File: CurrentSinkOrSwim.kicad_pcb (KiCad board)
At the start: 2 copper layers, 22 parts, among them P101 CONN_01X03, P102 CONN_01X02, P103 CONN_01X02, Q201 BUK9575, U201 LMV358, U401 LM2931D-R

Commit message: Rough board layout
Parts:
- added P201: CONN_01X01, CSOS Local:FA-220-38E, B.Cu at (116.8, 54.6)
- Q201: moved to B.Cu
- moved R303 69.3 mm to (99.1, 58.4)
- moved R301 65.1 mm to (99.1, 61.0), turned to 180 degrees
- moved R402 61.4 mm to (99.1, 44.5), turned to 270 degrees
- moved P103 57.3 mm to (124.5, 76.2), turned to 180 degrees
- moved R403 53.9 mm to (120.7, 50.8)
- moved P102 53.8 mm to (118.1, 76.2), turned to 180 degrees
- moved U401 53.0 mm to (105.4, 45.7), turned to 90 degrees
- moved R302 52.7 mm to (115.6, 50.8)
- moved P101 51.5 mm to (110.5, 76.2), turned to 180 degrees
- moved D301 45.7 mm to (125.7, 44.5), turned to 180 degrees
- moved R201 43.3 mm to (105.4, 50.8)
- moved R202 43.1 mm to (100.3, 54.6)
- moved R401 42.4 mm to (120.7, 53.3), turned to 180 degrees
- moved C301 42.2 mm to (132.1, 47.0)
- moved C402 39.8 mm to (99.1, 64.8)
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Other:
- board outline added: 43.2 x 41.9 mm

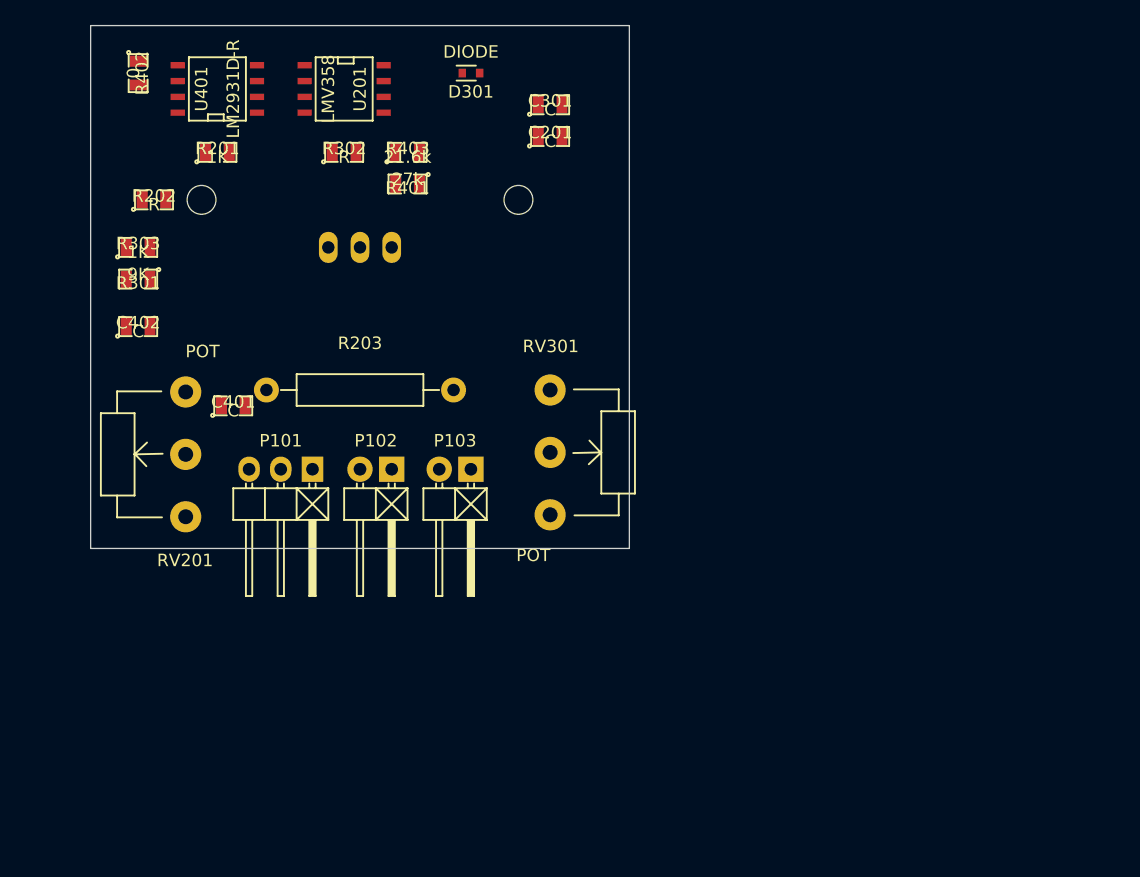
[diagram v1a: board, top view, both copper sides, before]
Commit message: Updated the POT references and schematic
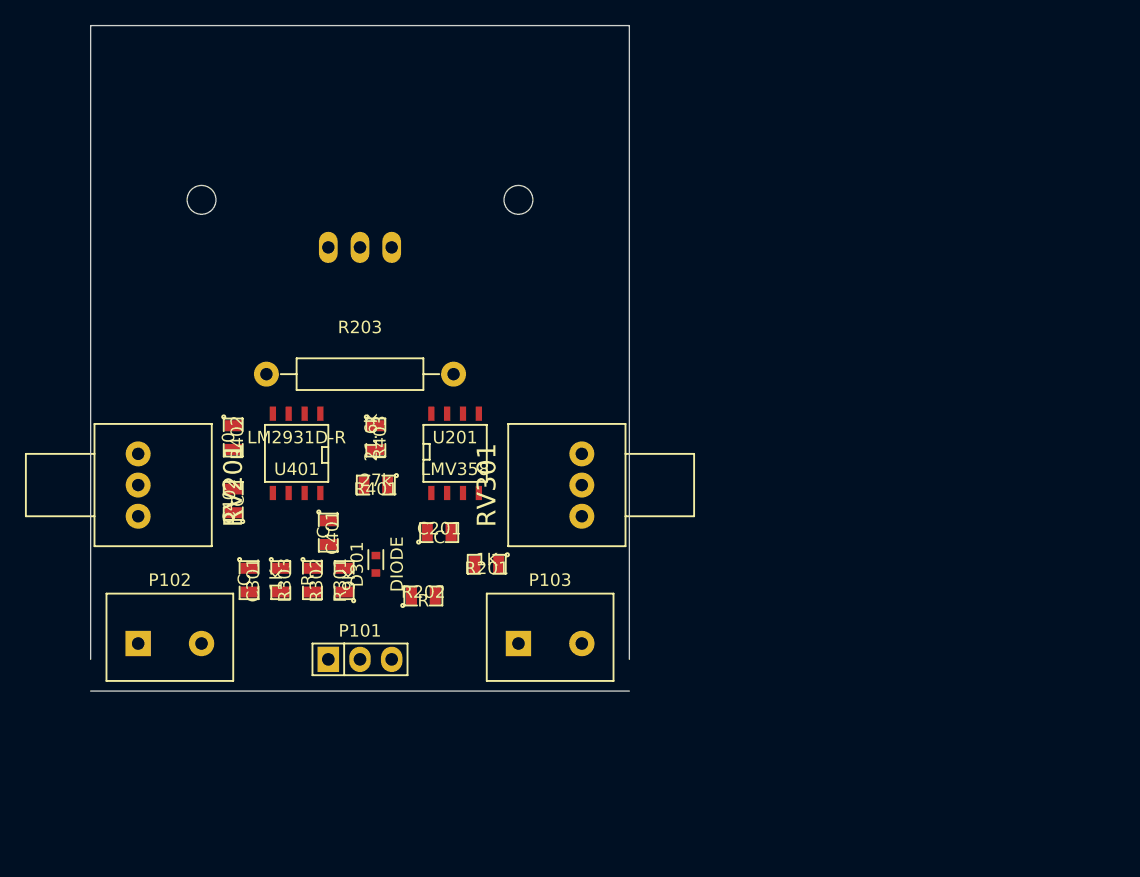
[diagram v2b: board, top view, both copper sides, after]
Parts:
- P101: footprint Pin_Headers:Pin_Header_Angled_1x03 -> Pin_Headers:Pin_Header_Straight_1x03
- P102, P103: footprint Pin_Headers:Pin_Header_Angled_1x02 -> CSOS Local:Terminal_Block_1x200_mil
- RV201, RV301: footprint Potentiometers:Potentiometer_WirePads_largePads -> CSOS Local:P090L-02F25BR10K
- moved C301 45.1 mm to (108.0, 85.1), turned to 270 degrees
- moved D301 40.1 mm to (118.1, 83.8), turned to 90 degrees
- moved R201 39.5 mm to (127.0, 83.8), turned to 180 degrees
- moved R202 38.4 mm to (121.9, 86.4)
- moved R302 34.4 mm to (113.0, 85.1), turned to 270 degrees
- moved C201 33.0 mm to (123.2, 81.3)
- moved U201 30.5 mm to (124.5, 74.9), turned to 0 degrees
- moved R402 30.2 mm to (106.7, 73.7)
- moved U401 29.9 mm to (111.8, 74.9), turned to 180 degrees
- moved R301 29.2 mm to (115.6, 85.1), turned to 90 degrees
- moved R303 29.0 mm to (110.5, 85.1), turned to 270 degrees
- moved R401 24.3 mm to (118.1, 77.5)
- moved R403 23.0 mm to (118.1, 73.7), turned to 270 degrees
- moved P102 21.6 mm to (101.6, 90.2), turned to 0 degrees
- moved P101 16.5 mm to (116.8, 91.4), turned to 0 degrees
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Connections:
- P102 pad 1: GND -> Net-(P101-Pad1)
- P102 pad 2: Net-(P101-Pad1) -> GND
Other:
- board size 43.2 x 41.9 mm -> 43.2 x 53.3 mm

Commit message: Initial layout
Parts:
- C201, C301, C401, C402: moved to B.Cu
- P201, Q201: moved to F.Cu
- moved RV301 35.2 mm to (99.6, 74.7), turned to 270 degrees
- moved RV201 35.2 mm to (134.1, 74.7), turned to 90 degrees
- moved R301 21.5 mm to (115.7, 63.6), turned to 270 degrees
- moved C301 21.3 mm to (129.2, 82.9), turned to 0 degrees
- moved R402 19.0 mm to (123.6, 82.3), turned to 90 degrees
- moved R403 14.0 mm to (123.7, 86.5)
- moved R302 12.7 mm to (111.6, 72.5)
- moved R303 12.6 mm to (109.3, 72.5)
- moved C402 12.3 mm to (119.0, 79.5), turned to 180 degrees
- moved C201 11.9 mm to (135.1, 81.0)
- moved R202 11.9 mm to (125.2, 74.9), turned to 180 degrees
- moved R401 11.5 mm to (110.1, 85.7), turned to 270 degrees
- moved R201 11.5 mm to (125.1, 72.5)
- moved U401 11.1 mm to (116.7, 84.8), turned to 270 degrees
- moved D301 9.62 mm to (111.0, 77.3), turned to 0 degrees
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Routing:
- added copper zone on B.Cu, net (none)
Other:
- board size 43.2 x 53.3 mm -> 41.7 x 50.8 mm

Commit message: First cut of layout in preperation for the final session
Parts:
- R202: value R -> 68K
- R302: value R -> 28.7K
- RV201, RV301: value POT -> 10K
- moved R403 13.7 mm to (111.1, 81.2)
- moved C201 8.01 mm to (127.1, 80.6)
- moved R402 4.21 mm to (123.2, 86.5)
- moved R401 3.23 mm to (107.8, 88.0)
- moved RV301 2.80 mm to (99.4, 77.5)
- moved RV201 2.67 mm to (134.1, 77.3)
- moved R303 2.16 mm to (107.8, 74.0)
- moved R302 1.91 mm to (110.5, 74.0)
- moved U201 1.78 mm to (118.1, 75.3)
- moved R203 1.26 mm to (116.3, 69.8), turned to 180 degrees
- moved C402 0.13 mm to (119.0, 79.4), turned to 0 degrees
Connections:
- R202 pad 1: Net-(R202-Pad1) -> 2.7V
- R202 pad 2: GND -> Net-(R202-Pad2)
- R301 pad 2: Net-(R301-Pad2) -> /Voltage Control/0-2v
- R302 pad 1: Net-(R302-Pad1) -> 2.7V
- R302 pad 2: GND -> /Voltage Control/0-2v
- R303 pad 1: Net-(R301-Pad2) -> /Voltage Control/0-2v
- R401 pad 1: Net-(R401-Pad1) -> 2.7V
- RV201 pad 1: Net-(RV201-Pad1) -> Net-(R202-Pad2)
- RV201 pad 2: 2.7V -> GND
- RV201 pad 3: Net-(R202-Pad1) -> Net-(RV201-Pad3)
- RV301 pad 2: 2.7V -> /Voltage Control/0-2v
- RV301 pad 3: Net-(R302-Pad1) -> GND
- U201 pad 3: Net-(R202-Pad1) -> Net-(R202-Pad2)
- U201 pad 5: Net-(R302-Pad1) -> /Voltage Control/0-2v
- U201 pad 6: Net-(R301-Pad2) -> /Voltage Control/0-2v
- U401 pad 1: Net-(U401-Pad1) -> 2.7V
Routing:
- net /Current Control/Current_Sink+: track 0.00 -> 68.0 mm
- net Net-(P101-Pad1): track 0.00 -> 17.2 mm
- net /Power Regulation/Vin: track 0.00 -> 10.2 mm
- added copper zone on B.Cu, net GND
- removed copper zone on B.Cu, net (none)
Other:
- net class Power added: clearance 0.3048, trace_width 0.6096, via_dia 1.143, via_drill 0.762

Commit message: Routing and fixing schematic checkpoint
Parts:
- removed C301: C, SMD_Packages:SMD-0805
- R203: footprint Resistors_ThroughHole:Resistor_Horizontal_RM15mm -> Resistors_ThroughHole:Resistor_Vertical_RM5mm
- R302: moved to B.Cu
- moved P102 33.9 mm to (134.6, 84.9), turned to 90 degrees
- moved C201 21.0 mm to (108.1, 71.8), turned to 270 degrees
- moved R301 20.6 mm to (101.2, 78.2), turned to 180 degrees
- moved RV201 20.1 mm to (117.7, 89.0), turned to 0 degrees
- moved R202 16.2 mm to (109.3, 78.2), turned to 270 degrees
- moved U201 16.2 mm to (102.0, 74.0)
- moved P103 15.5 mm to (134.6, 74.5), turned to 90 degrees
- moved C401 15.3 mm to (120.8, 74.0)
- moved P101 15.3 mm to (128.7, 81.0), turned to 90 degrees
- moved R201 13.5 mm to (113.5, 65.5), turned to 270 degrees
- moved RV301 12.5 mm to (103.6, 89.3), turned to 0 degrees
- moved D301 12.2 mm to (110.7, 65.2), turned to 270 degrees
- moved R401 10.5 mm to (111.6, 78.2)
- moved R303 9.43 mm to (101.2, 80.8), turned to 0 degrees
- moved R402 6.18 mm to (124.2, 80.4)
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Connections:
- R301 pad 2: /Voltage Control/0-2v -> /Voltage Control/0-2v_FeedBack
- R303 pad 1: /Voltage Control/0-2v -> /Voltage Control/0-2v_FeedBack
- U201 pad 6: /Voltage Control/0-2v -> /Voltage Control/0-2v_FeedBack
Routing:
- net /Current Control/Current_Sink+: track 68.0 -> 34.3 mm
- net /Current Control/FET_GATE: track 0.00 -> 14.0 mm
- net /Voltage Control/0-2v: track 0.00 -> 14.0 mm
- net GND: track 0.00 -> 13.8 mm, vias 0 -> 1
- net Net-(P101-Pad1): track 17.2 -> 7.51 mm
- net Net-(Q201-PadS): track 0.00 -> 7.81 mm
- net 2.7V: track 0.00 -> 5.57 mm, vias 0 -> 1
- net /Power Regulation/Vin: track 10.2 -> 15.8 mm, vias 0 -> 1
- net Net-(R402-Pad1): track 0.00 -> 3.46 mm

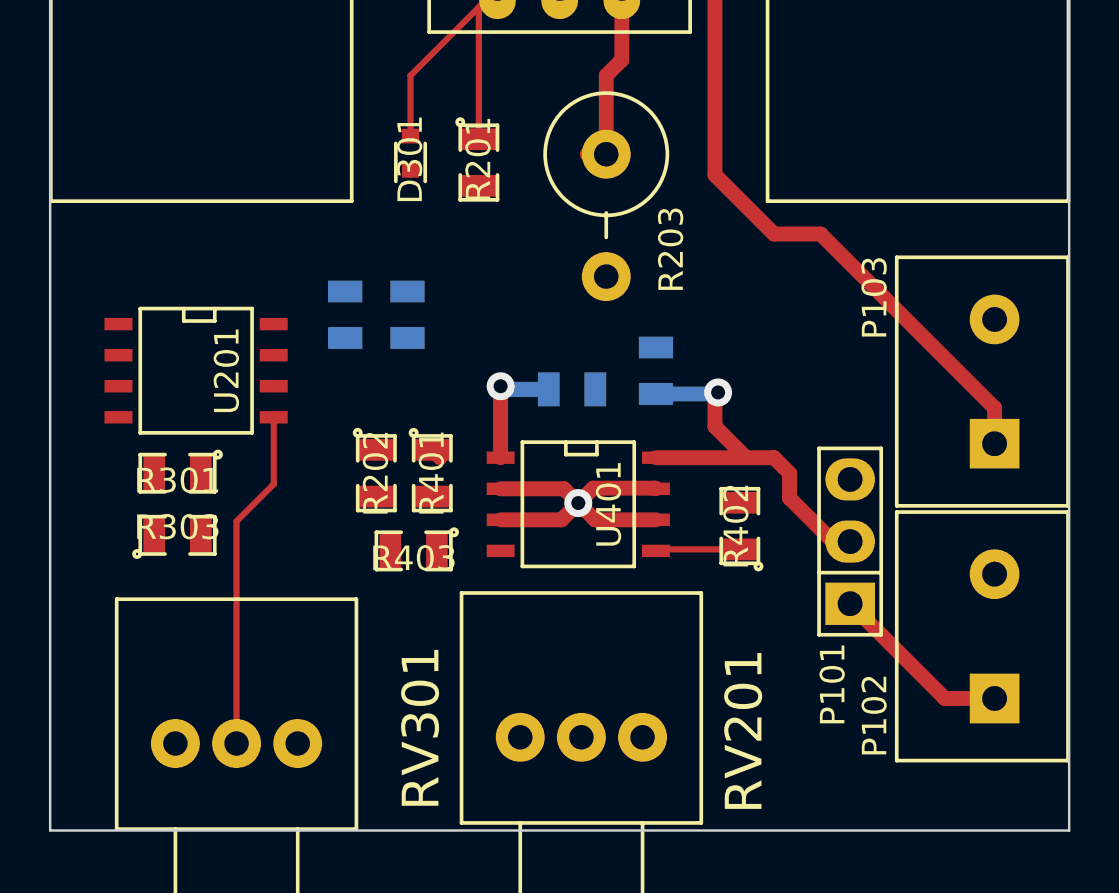
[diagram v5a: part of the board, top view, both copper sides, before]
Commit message: Initial route before filling the ground plane
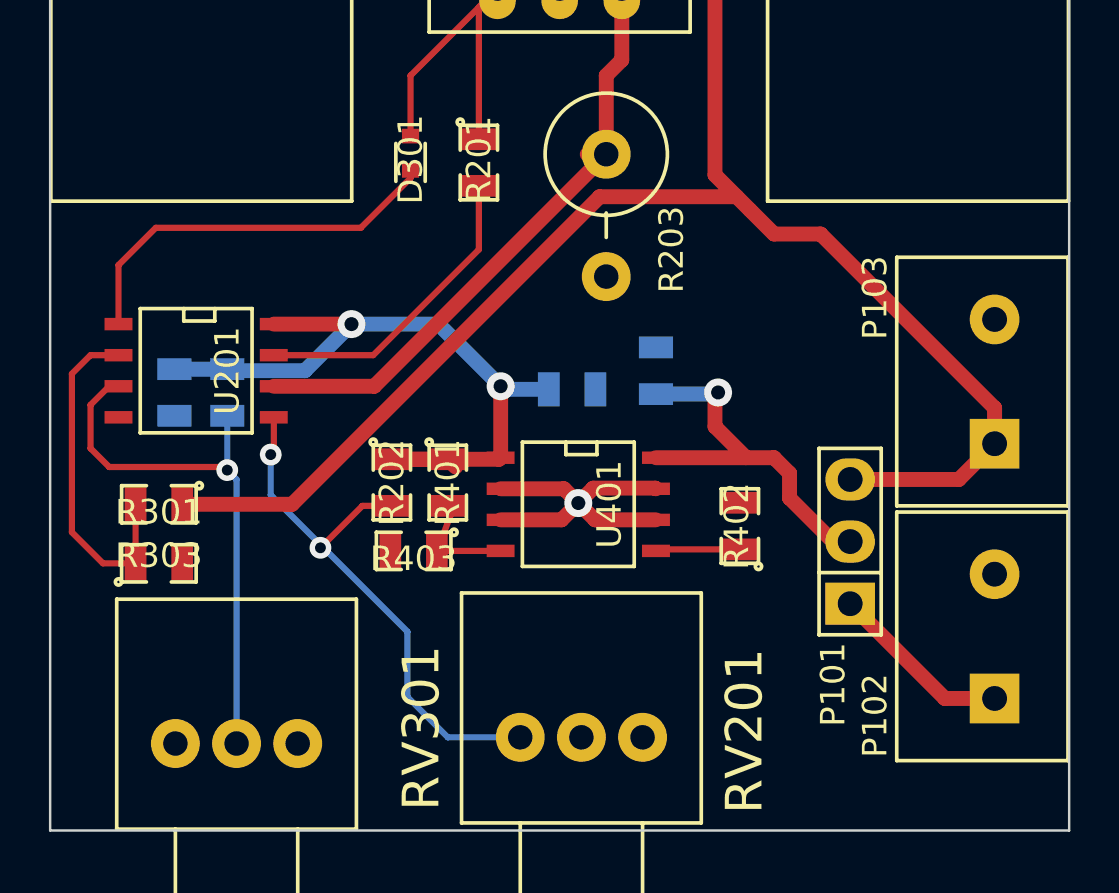
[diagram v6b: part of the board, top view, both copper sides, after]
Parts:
- moved R302 8.02 mm to (103.3, 74.9)
- moved C201 7.67 mm to (101.1, 74.9)
- moved R301 1.48 mm to (100.5, 79.5)
- moved R303 1.37 mm to (100.5, 81.9)
- moved R202 0.74 mm to (110.0, 78.6)
- moved R401 0.74 mm to (112.3, 78.6)
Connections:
- U201 pad 1: Net-(R201-Pad2) -> Net-(D301-Pad2)
- U201 pad 2: Net-(Q201-PadS) -> /Voltage Control/0-2v_FeedBack
- U201 pad 3: Net-(R202-Pad2) -> /Voltage Control/0-2v
- U201 pad 5: /Voltage Control/0-2v -> Net-(R202-Pad2)
- U201 pad 6: /Voltage Control/0-2v_FeedBack -> Net-(Q201-PadS)
- U201 pad 7: Net-(D301-Pad2) -> Net-(R201-Pad2)
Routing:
- net /Current Control/Current_Sink+: track 34.3 -> 68.7 mm
- net 2.7V: track 5.57 -> 30.7 mm, vias 1 -> 2
- net Net-(R202-Pad2): track 0.00 -> 23.0 mm, vias 0 -> 2
- net Net-(Q201-PadS): track 7.81 -> 25.3 mm
- net Net-(D301-Pad2): track 0.19 -> 16.3 mm
- net /Voltage Control/0-2v_FeedBack: track 0.18 -> 14.4 mm
- net Net-(R201-Pad2): track 0.00 -> 12.8 mm
- net /Voltage Control/0-2v: track 14.0 -> 22.8 mm, vias 0 -> 1
- net Net-(R401-Pad2): track 0.45 -> 5.09 mm

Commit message: Routed and filled board
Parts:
- moved C402 1.40 mm to (117.2, 73.4)
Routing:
- net GND: track 13.8 -> 24.0 mm, vias 1 -> 4
- net /Voltage Control/0-2v: track 22.8 -> 25.6 mm
- net /Current Control/FET_GATE: track 14.0 -> 12.4 mm
- net 2.7V: track 30.7 -> 31.4 mm
